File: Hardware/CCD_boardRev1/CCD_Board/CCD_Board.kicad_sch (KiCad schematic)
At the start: 13 parts

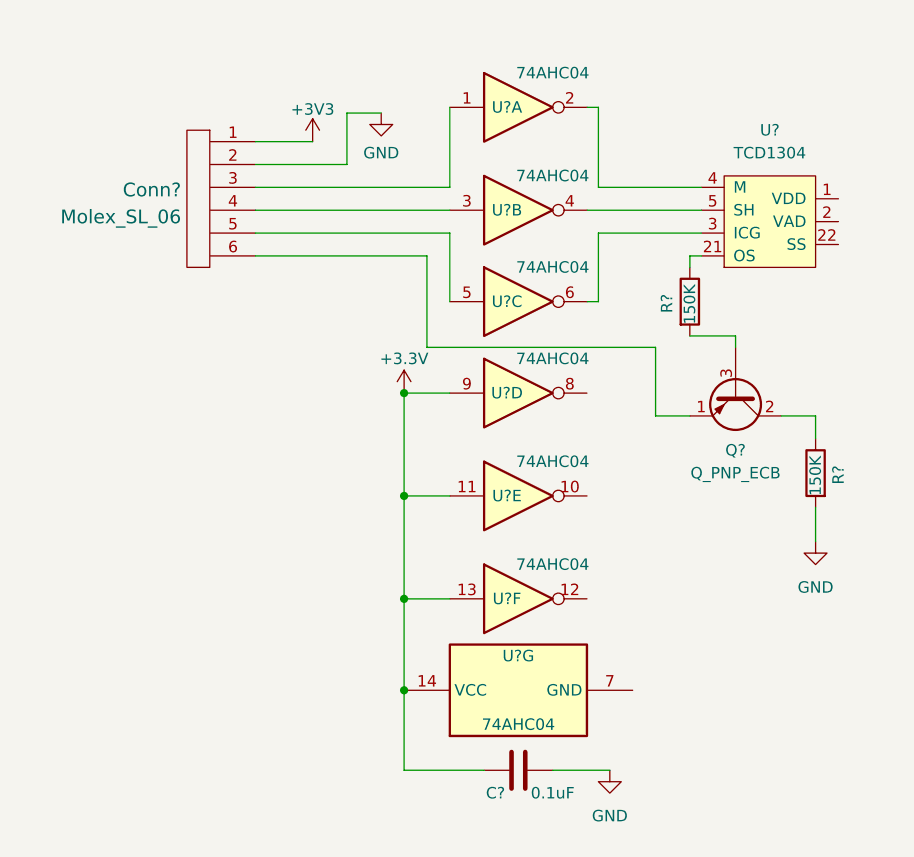
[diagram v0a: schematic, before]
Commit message: Finished Fluoro-board Schematic
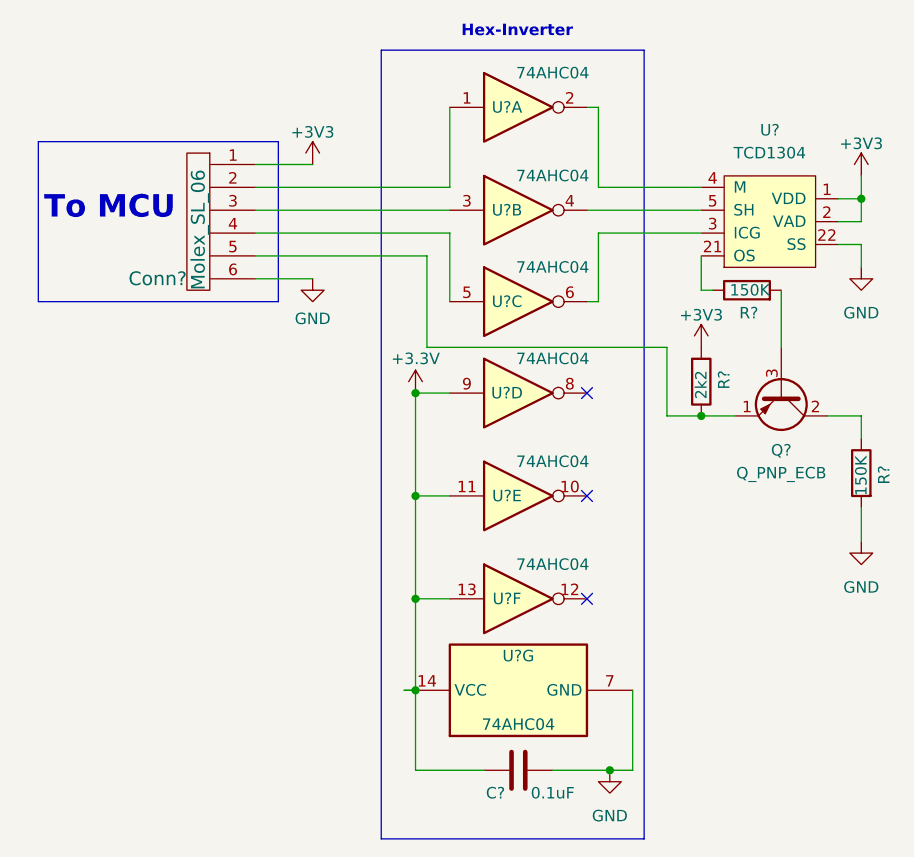
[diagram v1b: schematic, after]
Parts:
- removed Conn?: Molex_SL_06, Connector_Molex:Molex_SL_171971-0006_1x06_P2.54mm_Vertical, symbol Molex_SL_06:Molex_SL_06
- added Conn?: Molex_SL_06, Connector_Molex:Molex_SL_171971-0006_1x06_P2.54mm_Vertical, symbol Molex_SL_06:Molex_SL_06
- added R?: 2k2, symbol Device:R
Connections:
- net +3V3: now also U?.1 (VDD), U?.2 (VAD), Conn?.1, R?.2
- net GND: now also U?.22 (SS), U?.7 (GND), Conn?.6
- net at U?.1: now also Conn?.2
- net at U?.3: now also Conn?.3
- net at U?.5: now also Conn?.4
- net at Q?.1 (E): now also Conn?.5, R?.1
- no-connect marks 0 -> 3
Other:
- note added: "Hex-Inverter"
- note added: "To MCU"
- moved on the sheet: Q?, R?

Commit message: Finished CCD Board Layout
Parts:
- added H1, H2, H3, H4: MountingHole, MRDT_Drill_Holes:4_40_Hole_Corner, symbol Mechanical:MountingHole
- C1: renamed from C?; footprint (none) -> Capacitor_SMD:C_0603_1608Metric
- Q1: renamed from Q?; footprint (none) -> Package_TO_SOT_THT:TO-92
- R1, R2, R3: renamed from R?; footprint (none) -> Resistor_SMD:R_0603_1608Metric
- U1: renamed from U?; footprint (none) -> Package_SO:SOIC-14_3.9x8.7mm_P1.27mm
- U2: renamed from U?; footprint (none) -> MRDT_Sensors:TCD-1304
- gave numbers to parts that had none: 1
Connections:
- net +3.3V is gone; now on net +3V3: C1.2, U1.11, U1.13, U1.14 (VCC), U1.9

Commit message: Finalizing schematic component placement
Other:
- moved on the sheet: H1, H2, H3, H4
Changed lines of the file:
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@@
     (pin "1")
   )
-  (symbol (lib_id "Mechanical:MountingHole") (at 93.98 116.84 0) (unit 1)
-    (in_bom yes) (on_board yes) (fields_autoplaced)
-    (property "Reference" "H4" (id 0) (at 96.52 115.5699 0)
-      (effects (font (size 1.27 1.27)) (justify left))
-    )
-    (property "Value" "MountingHole" (id 1) (at 96.52 118.1099 0)
-      (effects (font (size 1.27 1.27)) (justify left))
-    )
-    (property "Footprint" "MRDT_Drill_Holes:4_40_Hole_Corner" (id 2) (at 93.98 116.84 0)
-      (effects (font (size 1.27 1.27)) hide)
-    )
-    (property "Datasheet" "~" (id 3) (at 93.98 116.84 0)
+  (symbol (lib_id "Mechanical:MountingHole") (at 85.09 110.49 0) (unit 1)
+    (in_bom yes) (on_board yes) (fields_autoplaced)
+    (property "Reference" "H4" (id 0) (at 87.63 109.2199 0)
+      (effects (font (size 1.27 1.27)) (justify left))
+    )
+    (property "Value" "MountingHole" (id 1) (at 87.63 111.7599 0)
+      (effects (font (size 1.27 1.27)) (justify left))
+    )
+    (property "Footprint" "MRDT_Drill_Holes:4_40_Hole_Corner" (id 2) (at 85.09 110.49 0)
+      (effects (font (size 1.27 1.27)) hide)
+    )
+    (property "Datasheet" "~" (id 3) (at 85.09 110.49 0)
       (effects (font (size 1.27 1.27)) hide)
     )
@@
     (pin "7")
   )
-  (symbol (lib_id "Mechanical:MountingHole") (at 93.98 106.68 0) (unit 1)
-    (in_bom yes) (on_board yes) (fields_autoplaced)
-    (property "Reference" "H2" (id 0) (at 96.52 105.4099 0)
-      (effects (font (size 1.27 1.27)) (justify left))
-    )
-    (property "Value" "MountingHole" (id 1) (at 96.52 107.9499 0)
-      (effects (font (size 1.27 1.27)) (justify left))
-    )
-    (property "Footprint" "MRDT_Drill_Holes:4_40_Hole_Corner" (id 2) (at 93.98 106.68 0)
-      (effects (font (size 1.27 1.27)) hide)
-    )
-    (property "Datasheet" "~" (id 3) (at 93.98 106.68 0)
+  (symbol (lib_id "Mechanical:MountingHole") (at 85.09 100.33 0) (unit 1)
+    (in_bom yes) (on_board yes) (fields_autoplaced)
+    (property "Reference" "H2" (id 0) (at 87.63 99.0599 0)
+      (effects (font (size 1.27 1.27)) (justify left))
+    )
+    (property "Value" "MountingHole" (id 1) (at 87.63 101.5999 0)
+      (effects (font (size 1.27 1.27)) (justify left))
+    )
+    (property "Footprint" "MRDT_Drill_Holes:4_40_Hole_Corner" (id 2) (at 85.09 100.33 0)
+      (effects (font (size 1.27 1.27)) hide)
+    )
+    (property "Datasheet" "~" (id 3) (at 85.09 100.33 0)
       (effects (font (size 1.27 1.27)) hide)
     )
@@
     (pin "2")
   )
-  (symbol (lib_id "Mechanical:MountingHole") (at 93.98 111.76 0) (unit 1)
-    (in_bom yes) (on_board yes) (fields_autoplaced)
-    (property "Reference" "H3" (id 0) (at 96.52 110.4899 0)
-      (effects (font (size 1.27 1.27)) (justify left))
-    )
-    (property "Value" "MountingHole" (id 1) (at 96.52 113.0299 0)
-      (effects (font (size 1.27 1.27)) (justify left))
-    )
-    (property "Footprint" "MRDT_Drill_Holes:4_40_Hole_Corner" (id 2) (at 93.98 111.76 0)
-      (effects (font (size 1.27 1.27)) hide)
-    )
-    (property "Datasheet" "~" (id 3) (at 93.98 111.76 0)
+  (symbol (lib_id "Mechanical:MountingHole") (at 85.09 105.41 0) (unit 1)
+    (in_bom yes) (on_board yes) (fields_autoplaced)
+    (property "Reference" "H3" (id 0) (at 87.63 104.1399 0)
+      (effects (font (size 1.27 1.27)) (justify left))
+    )
+    (property "Value" "MountingHole" (id 1) (at 87.63 106.6799 0)
+      (effects (font (size 1.27 1.27)) (justify left))
+    )
+    (property "Footprint" "MRDT_Drill_Holes:4_40_Hole_Corner" (id 2) (at 85.09 105.41 0)
+      (effects (font (size 1.27 1.27)) hide)
+    )
+    (property "Datasheet" "~" (id 3) (at 85.09 105.41 0)
       (effects (font (size 1.27 1.27)) hide)
     )
@@
     (pin "2")
   )
-  (symbol (lib_id "Mechanical:MountingHole") (at 93.98 101.6 0) (unit 1)
-    (in_bom yes) (on_board yes) (fields_autoplaced)
-    (property "Reference" "H1" (id 0) (at 96.52 100.3299 0)
-      (effects (font (size 1.27 1.27)) (justify left))
-    )
-    (property "Value" "MountingHole" (id 1) (at 96.52 102.8699 0)
-      (effects (font (size 1.27 1.27)) (justify left))
-    )
-    (property "Footprint" "MRDT_Drill_Holes:4_40_Hole_Corner" (id 2) (at 93.98 101.6 0)
-      (effects (font (size 1.27 1.27)) hide)
-    )
-    (property "Datasheet" "~" (id 3) (at 93.98 101.6 0)
-      (effects (font (size 1.27 1.27)) hide)
-    )
+  (symbol (lib_id "Mechanical:MountingHole") (at 85.09 95.25 0) (unit 1)
+    (in_bom yes) (on_board yes) (fields_autoplaced)
+    (property "Reference" "H1" (id 0) (at 87.63 93.9799 0)
+      (effects (font (size 1.27 1.27)) (justify left))
+    )
+    (property "Value" "MountingHole" (id 1) (at 87.63 96.5199 0)
+      (effects (font (size 1.27 1.27)) (justify left))
+    )
+    (property "Footprint" "MRDT_Drill_Holes:4_40_Hole_Corner" (id 2) (at 85.09 95.25 0)
+      (effects (font (size 1.27 1.27)) hide)
+    )
+    (property "Datasheet" "~" (id 3) (at 85.09 95.25 0)
+      (effects (font (size 1.27 1.27)) hide)
+    )
